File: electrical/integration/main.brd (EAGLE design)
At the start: 168 x 104 mm, 115 parts

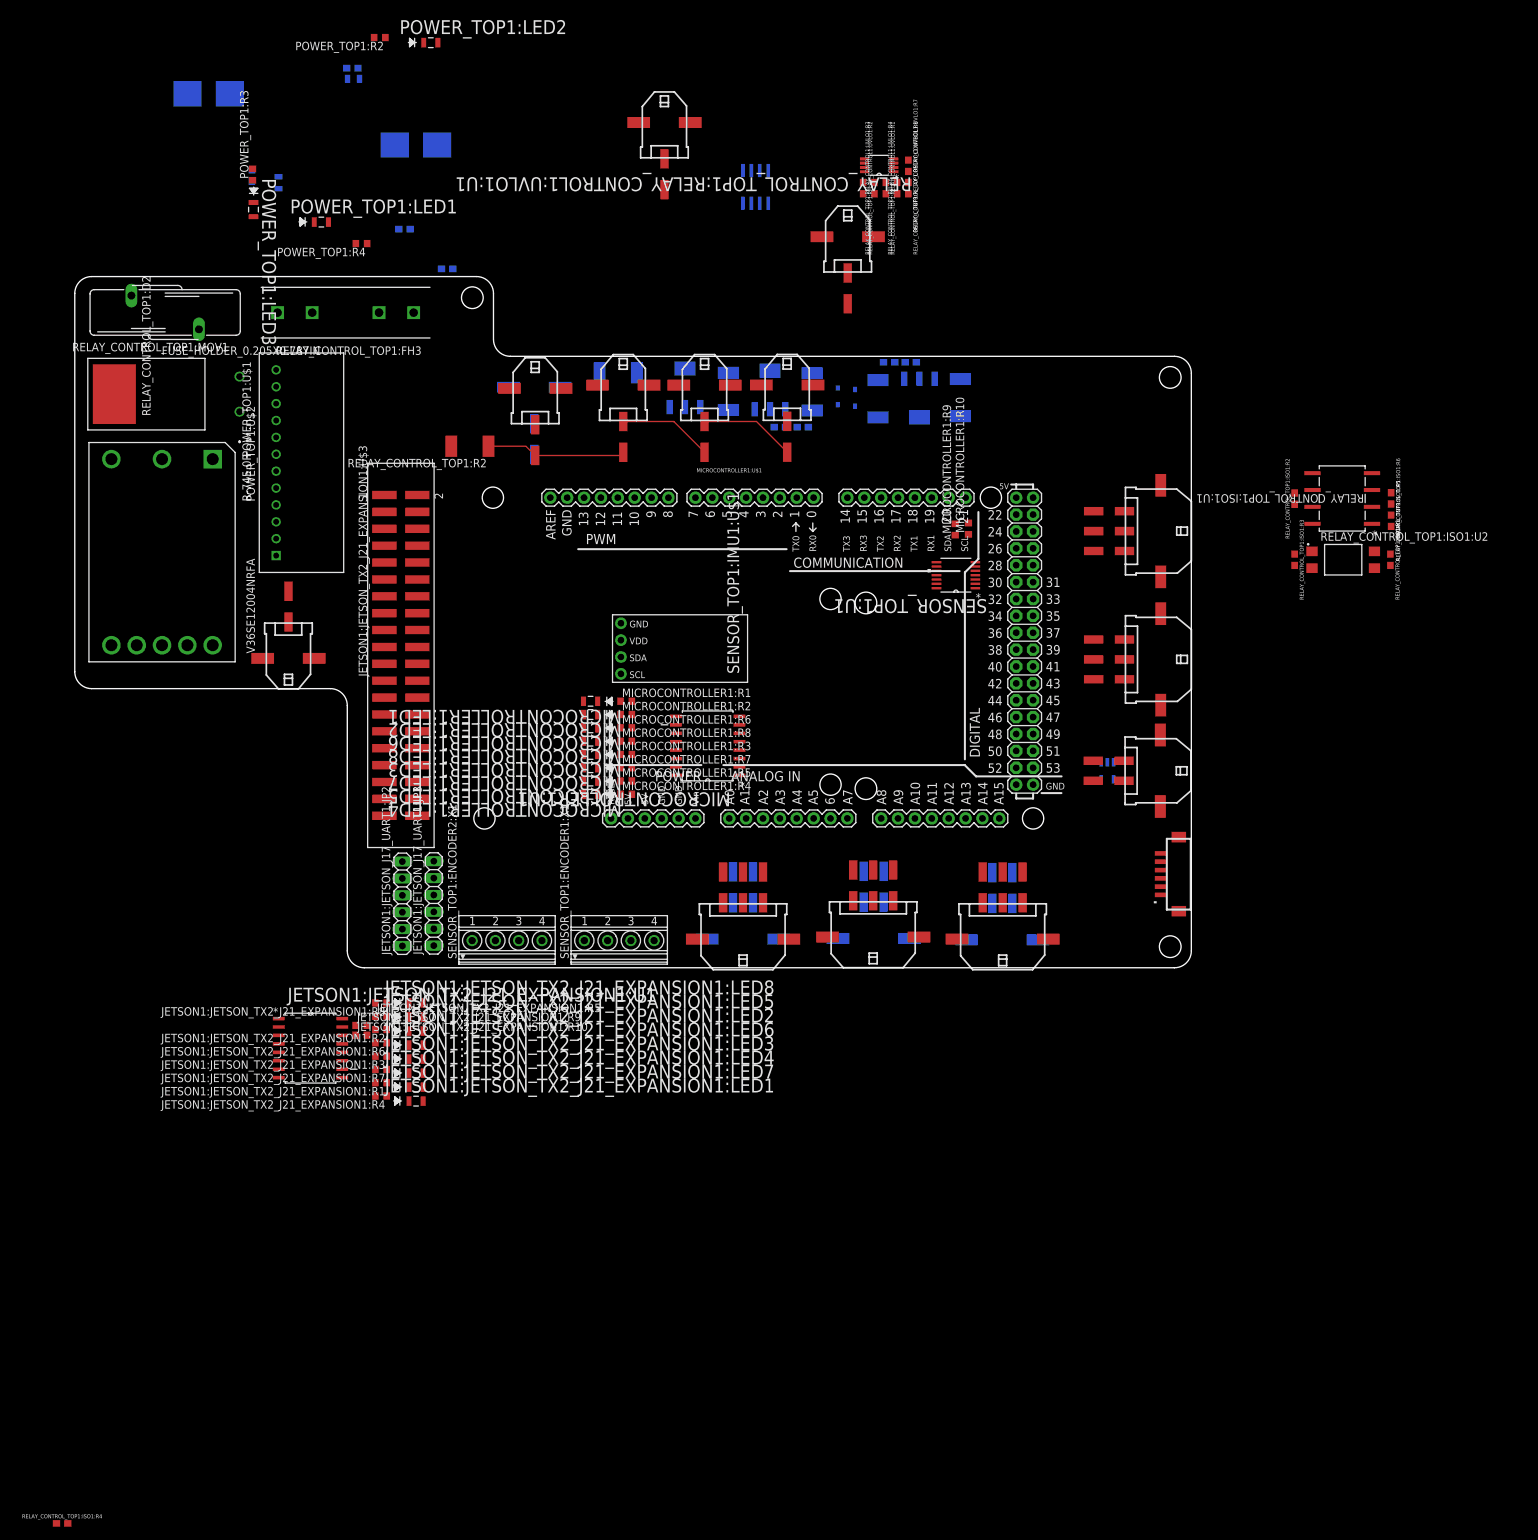
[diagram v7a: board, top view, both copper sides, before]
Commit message: 1st draft connector placement
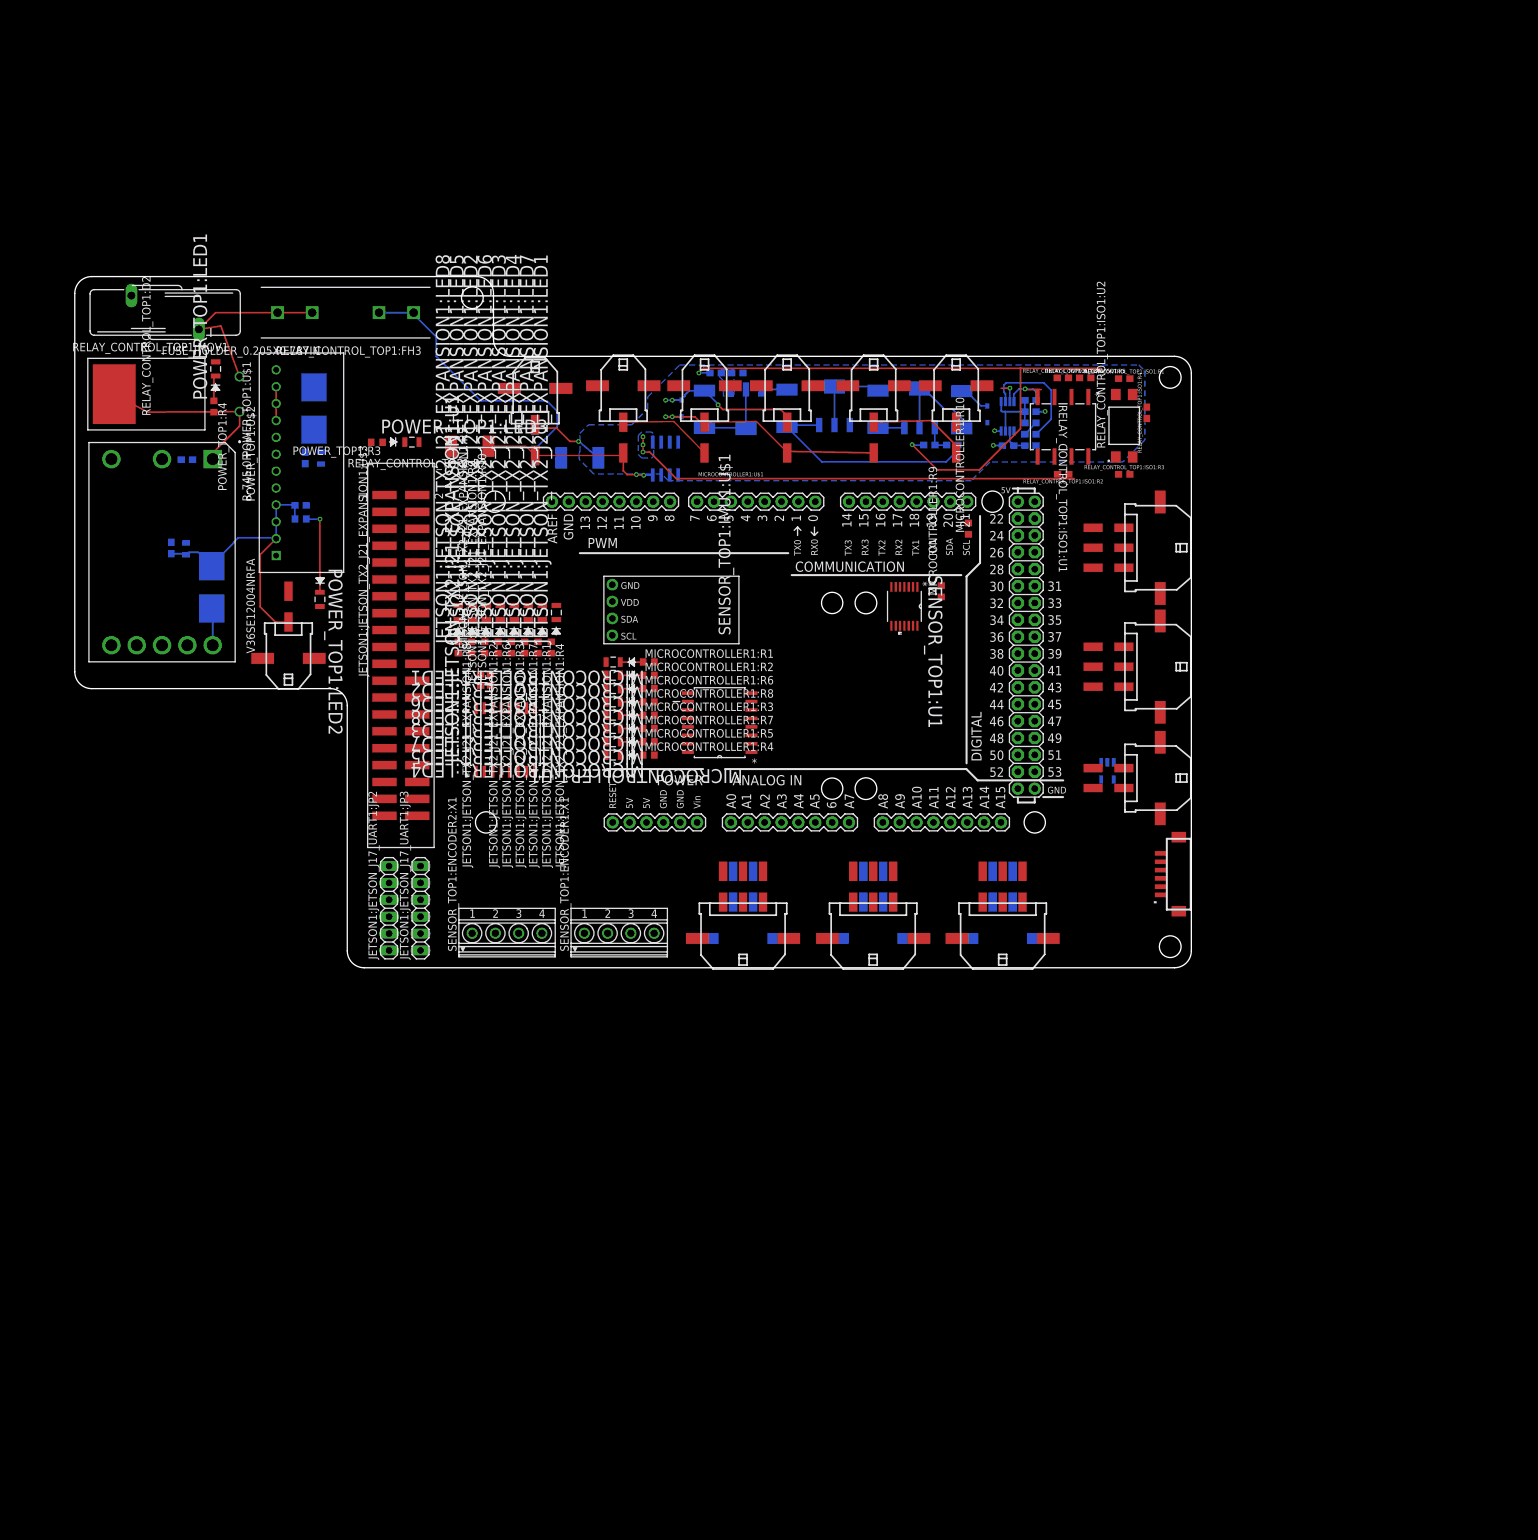
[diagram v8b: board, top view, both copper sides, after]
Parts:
- moved RELAY_CONTROL_TOP1:ISO1:R4 233.6 mm to (120.3, -8.50), turned to 90 degrees
- moved POWER_TOP1:LED2 85.4 mm to (-4.11, -36.6), turned to 270 degrees
- moved POWER_TOP1:C2 77.2 mm to (-26.5, -28.8), turned to 90 degrees
- moved JETSON1:JETSON_TX2_J21_EXPANSION1:LED1 76.5 mm to (31.5, -38.5), turned to 90 degrees
- moved POWER_TOP1:MOV1 75.1 mm to (-24.3, -29.0), turned to 90 degrees
- moved JETSON1:JETSON_TX2_J21_EXPANSION1:LED7 73.9 mm to (29.4, -38.5), turned to 90 degrees
- moved POWER_TOP1:R2 73.4 mm to (-7.02, -24.5), flipped to the bottom, turned to 0 degrees
- moved POWER_TOP1:F2 73.3 mm to (-20.4, -34.8), turned to 270 degrees
- moved JETSON1:JETSON_TX2_J21_EXPANSION1:R4 72.2 mm to (30.7, -43.8), turned to 270 degrees
- moved JETSON1:JETSON_TX2_J21_EXPANSION1:LED4 71.3 mm to (27.2, -38.5), turned to 90 degrees
- moved JETSON1:JETSON_TX2_J21_EXPANSION1:R1 69.6 mm to (28.7, -43.8), turned to 270 degrees
- moved JETSON1:JETSON_TX2_J21_EXPANSION1:LED3 68.8 mm to (25.1, -38.5), turned to 90 degrees
- moved JETSON1:JETSON_TX2_J21_EXPANSION1:R7 67.1 mm to (26.7, -43.8), turned to 270 degrees
- moved JETSON1:JETSON_TX2_J21_EXPANSION1:LED6 66.3 mm to (23.0, -38.5), turned to 90 degrees
- moved JETSON1:JETSON_TX2_J21_EXPANSION1:R3 64.5 mm to (24.7, -43.8), turned to 270 degrees
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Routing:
- net RELAY_CONTROL_TOP1:RELAY_CONTROL1:!UVLO!: track 0.00 -> 97.1 mm, vias 0 -> 3
- net 5V_ISO: track 0.00 -> 77.6 mm, vias 0 -> 4
- net GND_ISO: track 0.00 -> 50.3 mm, vias 0 -> 4
- net 12V: track 0.00 -> 45.4 mm
- net RELAY_CONTROL_TOP1:N$1: track 0.00 -> 42.8 mm
- net RELAY_CONTROL_TOP1:N$11: track 0.00 -> 29.5 mm
- net 36V: track 0.00 -> 27.8 mm
- net RELAY_CONTROL_TOP1:N$3: track 14.3 -> 37.7 mm, vias 0 -> 2
- net RELAY_CONTROL_TOP1:N$6: track 0.00 -> 21.7 mm, vias 0 -> 3
- net RELAY_CONTROL_TOP1:RELAY_CONTROL1:UVLO1:N$2: track 0.00 -> 17.8 mm
- net RELAY_CONTROL_TOP1:RELAY_CONTROL1:N$5: track 0.00 -> 15.6 mm
- net RELAY_CONTROL_TOP1:N$2: track 0.00 -> 14.2 mm
- net POWER_TOP1:N$4: track 0.00 -> 13.1 mm, vias 0 -> 1
- net RELAY_CONTROL_TOP1:RELAY_CONTROL1:N$2: track 0.00 -> 12.6 mm
- net RELAY_CONTROL_TOP1:RELAY_CONTROL1:N$10: track 0.00 -> 12.0 mm
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- added copper zone on layer 16, net 5V_ISO
- added copper zone on layer 16, net GND_ISO
- added copper zone on layer 16, net N$36
- added copper zone on layer 16, net RELAY_CONTROL_TOP1:RELAY_CONTROL1:N$7
